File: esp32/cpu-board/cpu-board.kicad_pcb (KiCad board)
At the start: 2 copper layers, 99.9 x 69.8 mm, 61 parts, among them J1 Conn_01x06, J2 Conn_01x08, J3 Conn_01x10, J4 Conn_01x10, J5 Conn_01x06, Q1 IRLI640G, Q2 PMBTA42DS,125, Q3 PMBTA42DS,125, Q4 PMBTA42DS,125, Q5 PMBTA42DS,125, Q6 PMBTA42DS,125, U1 ESP32-DevBoard2, U2 MAX7320, U3 MAX7320, U4 MAX7320, U5 V7803-1000, U6 MAX1771

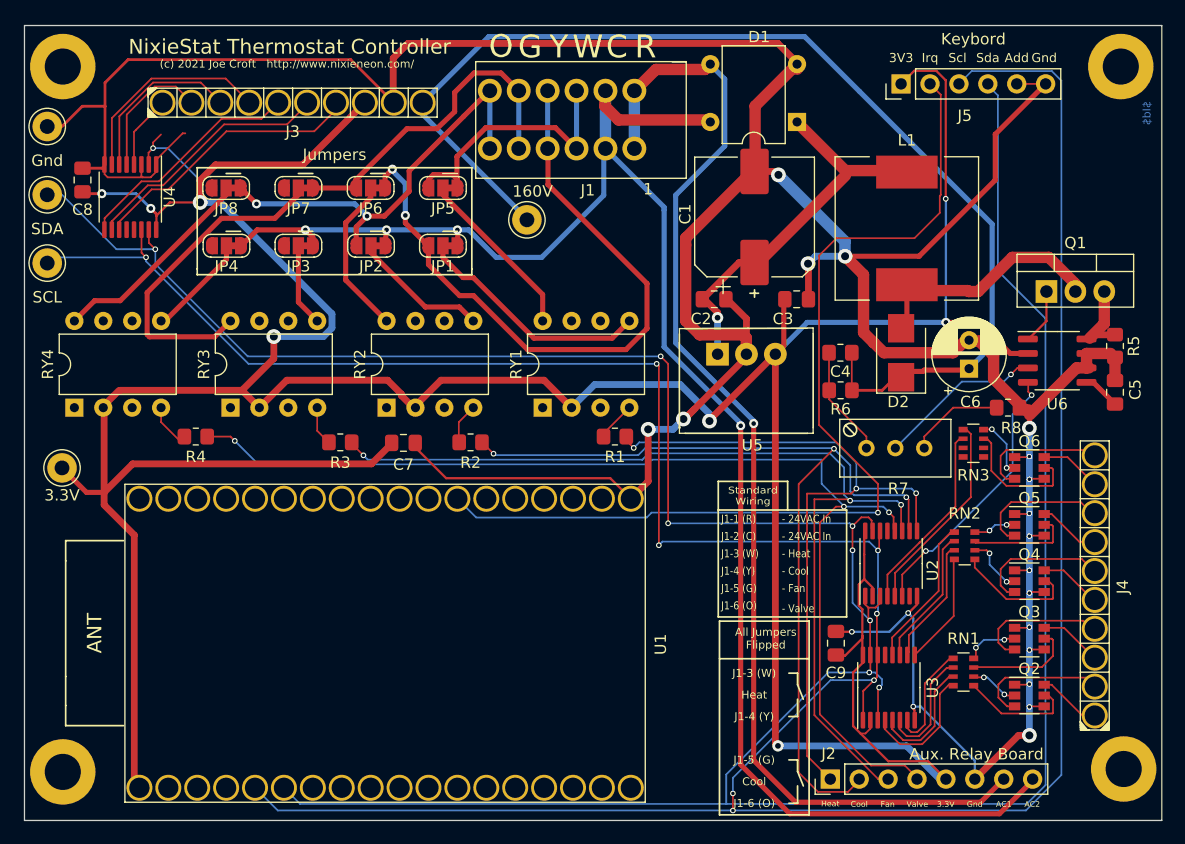
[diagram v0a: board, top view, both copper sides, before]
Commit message: Added ground connection, broke the schematic into two sheets
[git-p4: depot-paths = "//depot/nixiestat/": change = 316]
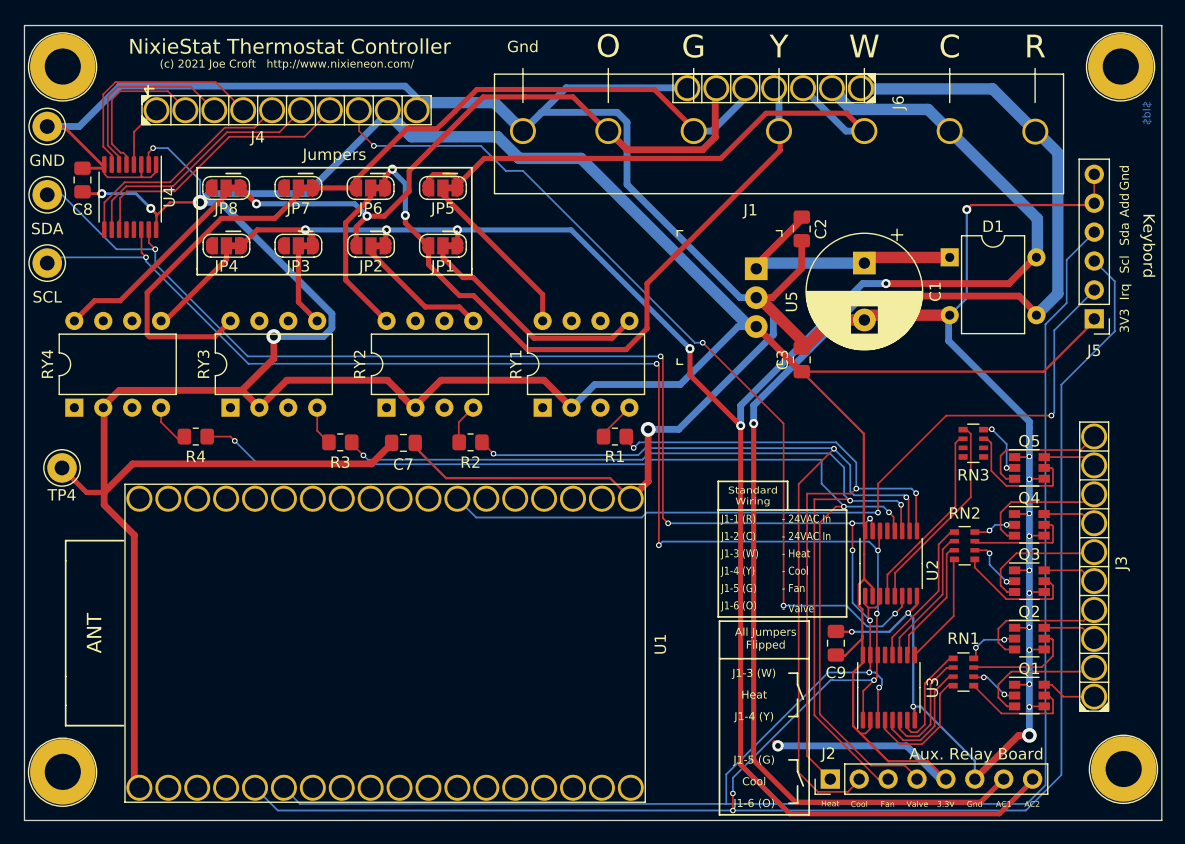
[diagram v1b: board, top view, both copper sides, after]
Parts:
- removed 160V: 160V, Connector_Pin:Pin_D1.3mm_L11.0mm
- removed C4: 2nf, Resistor_SMD:R_0805_2012Metric_Pad1.20x1.40mm_HandSolder
- removed C5: 1nf, Capacitor_SMD:C_0805_2012Metric_Pad1.18x1.45mm_HandSolder
- removed C6: 4.7uf 250V, Capacitor_THT:CP_Radial_D6.3mm_P2.50mm
- removed D2: MBRD102200CT, Diode_SMD:D_SMB
- removed L1: 150uh, Inductor_SMD:L_12x12mm_H8mm
- removed Q6: PMBTA42DS,125, Package_TO_SOT_SMD:SuperSOT-6
- removed R5: .1, Resistor_SMD:R_0805_2012Metric_Pad1.20x1.40mm_HandSolder
- removed R6: 1M, Resistor_SMD:R_0805_2012Metric_Pad1.20x1.40mm_HandSolder
- removed R7: 20K, Potentiometer_THT:Potentiometer_Bourns_3296W_Vertical
- removed R8: 1.2K, Resistor_SMD:R_0805_2012Metric_Pad1.20x1.40mm_HandSolder
- removed U6: MAX1771, Package_SO:SO-8_3.9x4.9mm_P1.27mm
- added J6: Conn_01x07, croftj:Mill-Max-295x7, F.Cu at (173.5, 81.4)
- C1: footprint Capacitor_SMD:CP_Elec_10x10 -> Capacitor_THT:CP_Radial_D10.0mm_P5.00mm
- J1: value Conn_01x06 -> Conn_01x07; footprint croftj:TES-1-2834015-6 -> croftj:conn-phx-1703090
- Q1: value IRLI640G -> PMBTA42DS,125; footprint Package_TO_SOT_THT:TO-220-3_Vertical -> Package_TO_SOT_SMD:SuperSOT-6
- moved J4 103.0 mm to (104.0, 80.8), turned to 90 degrees
- moved J3 102.0 mm to (188.9, 137.4), turned to 180 degrees
- moved Q1 35.5 mm to (184.5, 133.5)
- moved J5 26.7 mm to (190.2, 100.4), turned to 180 degrees
- moved D1 17.9 mm to (177.5, 95.0), turned to 0 degrees
- moved J1 16.6 mm to (160.0, 89.4)
- moved C1 10.5 mm to (170.0, 95.5), turned to 270 degrees
- moved C2 9.87 mm to (164.5, 92.5), turned to 270 degrees
- moved U5 8.24 mm to (160.5, 96.0), turned to 270 degrees
- moved C3 5.34 mm to (164.5, 104.0), turned to 90 degrees
- moved Q3 5.05 mm to (184.5, 123.5)
- moved Q2 5.00 mm to (184.5, 128.5)
- moved Q5 5.00 mm to (184.5, 113.5)
- moved Q4 4.95 mm to (184.5, 118.5)
- renumbered Gnd to GND, 3.3V to TP4
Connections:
- J3 pad 1: DIG1 -> SEG_D_1
- J3 pad 10: +160V -> SEG_D_10
- J3 pad 2: DIG2 -> SEG_D_2
- J3 pad 3: DIG3 -> SEG_D_3
- J3 pad 4: DIG4 -> SEG_D_4
- J3 pad 5: DIG5 -> SEG_D_5
- J3 pad 6: DIG6 -> SEG_D_6
- J3 pad 7: DIG7 -> SEG_D_7
- J3 pad 8: +3.3V -> SEG_D_8
- J3 pad 9: GNDREF -> SEG_D_9
- J4 pad 1: SEG_D_1 -> Net-(J4-Pad1)
- J4 pad 10: SEG_D_10 -> GNDREF
- J4 pad 2: SEG_D_2 -> Net-(J4-Pad2)
- J4 pad 3: SEG_D_3 -> Net-(J4-Pad3)
- J4 pad 4: SEG_D_4 -> Net-(J4-Pad4)
- J4 pad 5: SEG_D_5 -> Net-(J4-Pad5)
- J4 pad 6: SEG_D_6 -> Net-(J4-Pad6)
- J4 pad 7: SEG_D_7 -> Net-(J4-Pad7)
- J4 pad 8: SEG_D_8 -> ~HV_EN~
- J4 pad 9: SEG_D_9 -> +3.3V
- Q1 pad 1: Net-(Q1-Pad1) -> GNDREF
- Q1 pad 2: Net-(D2-Pad2) -> SEG2
- Q1 pad 3: Net-(Q1-Pad3) -> SEG_D_2
- Q2 pad 2: SEG2 -> SEG4
- Q2 pad 3: SEG_D_2 -> SEG_D_4
- Q2 pad 5: SEG1 -> SEG3
- Q2 pad 6: SEG_D_1 -> SEG_D_3
- Q3 pad 2: SEG4 -> SEG6
- Q3 pad 3: SEG_D_4 -> SEG_D_6
- Q3 pad 5: SEG3 -> SEG5
- Q3 pad 6: SEG_D_3 -> SEG_D_5
- Q4 pad 2: SEG6 -> SEG8
- Q4 pad 3: SEG_D_6 -> SEG_D_8
- Q4 pad 5: SEG5 -> SEG7
- Q4 pad 6: SEG_D_5 -> SEG_D_7
- Q5 pad 2: SEG8 -> SEG10
- Q5 pad 3: SEG_D_8 -> SEG_D_10
- Q5 pad 5: SEG7 -> SEG9
- Q5 pad 6: SEG_D_7 -> SEG_D_9
- U4 pad 10: DIG6 -> Net-(J4-Pad6)
- U4 pad 11: DIG7 -> Net-(J4-Pad7)
- U4 pad 4: DIG1 -> Net-(J4-Pad1)
- U4 pad 5: DIG2 -> Net-(J4-Pad2)
- U4 pad 6: DIG3 -> Net-(J4-Pad3)
- U4 pad 7: DIG4 -> Net-(J4-Pad4)
- U4 pad 9: DIG5 -> Net-(J4-Pad5)
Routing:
- net +160V: track 101.8 -> 0.00 mm
- net ~HV_EN~: track 23.8 -> 78.4 mm, vias 2 -> 4
- net GNDREF: track 338.6 -> 292.8 mm, vias 20 -> 16
- net AC2: track 148.2 -> 175.2 mm, vias 4 -> 6
- net Net-(J1-Pad3): track 24.4 -> 50.8 mm
- net DIG7: track 24.4 -> 0.00 mm
- net Net-(J4-Pad7): track 0.00 -> 24.3 mm
- net I2C_SCL: track 276.2 -> 253.4 mm
- net Net-(D2-Pad2): track 22.7 -> 0.00 mm
- net Net-(J4-Pad6): track 0.00 -> 22.3 mm
- net DIG6: track 22.2 -> 0.00 mm
- net Net-(J4-Pad5): track 0.00 -> 22.0 mm
- net Net-(J4-Pad4): track 0.00 -> 20.5 mm
- net DIG5: track 20.4 -> 0.00 mm
- net Net-(J1-Pad6): track 37.9 -> 57.5 mm
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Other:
- board text removed: "1"

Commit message: First attempt at ensuring proper grounding Added capacitor to the reset pin Extended the reset line to the IO extenders
[git-p4: depot-paths = "//depot/nixiestat/": change = 324]
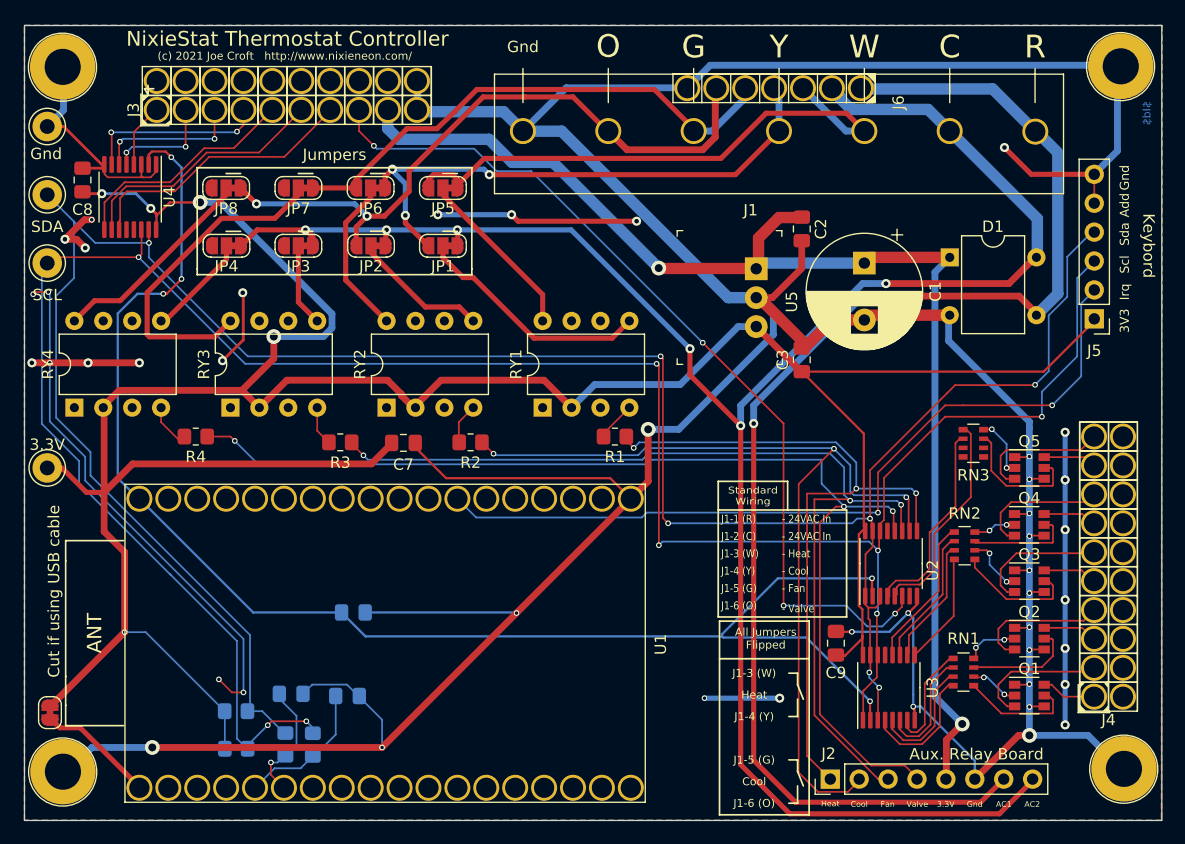
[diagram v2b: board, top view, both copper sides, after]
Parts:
- removed REF** (x4): 4-40-Screw, croftj:4-40-Screw
- added C4: .1uf, Capacitor_SMD:C_0805_2012Metric_Pad1.18x1.45mm_HandSolder, B.Cu at (125.1, 126.2)
- added C5: .1uf, Capacitor_SMD:C_0805_2012Metric_Pad1.18x1.45mm_HandSolder, B.Cu at (124.6, 133.5)
- added C6: .1uf, Capacitor_SMD:C_0805_2012Metric_Pad1.18x1.45mm_HandSolder, B.Cu at (119.6, 133.3)
- added JP9: Jumper_2_Bridged, Jumper:SolderJumper-2_P1.3mm_Bridged_RoundedPad1.0x1.5mm, F.Cu at (98.4, 135.0)
- added R5: 100K, Resistor_SMD:R_0805_2012Metric_Pad1.20x1.40mm_HandSolder, B.Cu at (114.8, 138.2)
- added R6: 100K, Resistor_SMD:R_0805_2012Metric_Pad1.20x1.40mm_HandSolder, B.Cu at (114.8, 134.9)
- added R7: 0 Ohm, Resistor_SMD:R_0805_2012Metric_Pad1.20x1.40mm_HandSolder, B.Cu at (121.5, 137.8)
- added R8: 0 Ohm, Resistor_SMD:R_0805_2012Metric_Pad1.20x1.40mm_HandSolder, B.Cu at (119.1, 137.8)
- added SH1: ScrewHole, croftj:4-40-Screw, F.Cu at (99.8, 73.8)
- added SH2: ScrewHole, croftj:4-40-Screw, F.Cu at (99.8, 135.7)
- added SH3: ScrewHole, croftj:4-40-Screw, F.Cu at (192.8, 73.8)
- added SH4: ScrewHole, croftj:4-40-Screw, F.Cu at (193.1, 135.5)
- J3: value Conn_01x10 -> Conn_02x10_Odd_Even; footprint croftj:Mill-Max-295x10 -> croftj:pcb_jack-2x10
- J4: value Conn_01x10 -> Conn_02x10_Odd_Even; footprint croftj:Mill-Max-295x10 -> croftj:pcb_jack-2x10-mirror
- moved J4 106.7 mm to (195.3, 136.1), turned to 180 degrees
- moved J3 100.3 mm to (105.3, 82.0), turned to 90 degrees
- moved TP4 1.30 mm to (98.2, 113.5)
- renumbered GND to TP1, SCL to TP2, SDA to TP3
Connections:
- C1 pad 1: Net-(C1-Pad1) -> VCC
- C2 pad 1: Net-(C1-Pad1) -> VCC
- D1 pad 1: Net-(C1-Pad1) -> VCC
- J2 pad 5: +3.3V -> VCC
- J3 pad 1: SEG_D_1 -> Net-(J3-Pad1)
- J3 pad 10: SEG_D_10 -> GNDREF
- J3 pad 2: SEG_D_2 -> GNDREF
- J3 pad 3: SEG_D_3 -> Net-(J3-Pad3)
- J3 pad 4: SEG_D_4 -> GNDREF
- J3 pad 5: SEG_D_5 -> Net-(J3-Pad5)
- J3 pad 6: SEG_D_6 -> GNDREF
- J3 pad 7: SEG_D_7 -> Net-(J3-Pad7)
- J3 pad 8: SEG_D_8 -> GNDREF
- J3 pad 9: SEG_D_9 -> Net-(J3-Pad9)
- J4 pad 1: Net-(J4-Pad1) -> SEG_D_1
- J4 pad 2: Net-(J4-Pad2) -> GNDREF
- J4 pad 3: Net-(J4-Pad3) -> SEG_D_2
- J4 pad 4: Net-(J4-Pad4) -> GNDREF
- J4 pad 5: Net-(J4-Pad5) -> SEG_D_3
- J4 pad 6: Net-(J4-Pad6) -> GNDREF
- J4 pad 7: Net-(J4-Pad7) -> SEG_D_4
- J4 pad 8: ~HV_EN~ -> GNDREF
- J4 pad 9: +3.3V -> SEG_D_5
- U1 pad 1: +3.3V -> Net-(JP9-Pad2)
- U1 pad 36: Net-(U1-Pad36) -> RESET
- U1 pad 5: I2C_SCL -> Net-(C5-Pad1)
- U1 pad 6: I2C_SDA -> Net-(C6-Pad1)
- U2 pad 2: +3.3V -> RESET
- U3 pad 2: +3.3V -> RESET
- U4 pad 10: Net-(J4-Pad6) -> Net-(J3-Pad11)
- U4 pad 11: Net-(J4-Pad7) -> Net-(J3-Pad13)
- U4 pad 2: +3.3V -> RESET
- U4 pad 4: Net-(J4-Pad1) -> Net-(J3-Pad1)
- U4 pad 5: Net-(J4-Pad2) -> Net-(J3-Pad3)
- U4 pad 6: Net-(J4-Pad3) -> Net-(J3-Pad5)
- U4 pad 7: Net-(J4-Pad4) -> Net-(J3-Pad7)
- U4 pad 9: Net-(J4-Pad5) -> Net-(J3-Pad9)
- U5 pad 1: Net-(C1-Pad1) -> VCC
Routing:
- net GNDREF: track 292.8 -> 477.7 mm, vias 16 -> 35
- net RESET: track 0.00 -> 127.5 mm, vias 0 -> 5
- net VCC: track 0.00 -> 111.4 mm, vias 0 -> 2
- net +3.3V: track 342.5 -> 280.0 mm, vias 6 -> 14
- net I2C_SDA: track 256.7 -> 207.9 mm, vias 9 -> 7
- net I2C_SCL: track 253.4 -> 207.8 mm
- net Net-(J3-Pad13): track 0.00 -> 24.3 mm
- net Net-(J4-Pad7): track 24.3 -> 0.00 mm
- net Net-(C1-Pad1): track 23.0 -> 0.00 mm
- net Net-(J4-Pad6): track 22.3 -> 0.00 mm
- net Net-(J3-Pad11): track 0.00 -> 22.3 mm
- net Net-(J4-Pad5): track 22.0 -> 0.00 mm
- net Net-(J4-Pad4): track 20.5 -> 0.00 mm
- net Net-(J3-Pad9): track 0.00 -> 20.3 mm
- net Net-(J4-Pad3): track 16.8 -> 0.00 mm
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- added copper zone on F.Cu, net +3.3V
- added copper zone on B.Cu, net GNDREF
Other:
- board text added: "Cut if using USB cable"
